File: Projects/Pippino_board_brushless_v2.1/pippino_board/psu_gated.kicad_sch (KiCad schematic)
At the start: 11 parts, among them Q1 2N3904, Q2 AO4409

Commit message: changed 5v buck to smaller one
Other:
- sheet PSU_5v0 ports: added 5V_EN; removed none
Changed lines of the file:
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@@
+    (stroke (width 0) (type default))
+  )
+  (wire (pts (xy 195.58 87.63) (xy 204.47 87.63))
     (stroke (width 0) (type default))
   )
@@
   (hierarchical_label "power_maintain" (shape input) (at 147.32 99.06 0) (fields_autoplaced)
     (effects (font (size 1.27 1.27)) (justify left))
+  )
+  (hierarchical_label "5V_EN" (shape input) (at 195.58 87.63 180) (fields_autoplaced)
+    (effects (font (size 1.27 1.27)) (justify right))
   )
   (hierarchical_label "trigger_manual" (shape input) (at 100.33 83.82 180) (fields_autoplaced)
@@
     )
   )
-  (sheet (at 204.47 81.28) (size 15.24 7.62) (fields_autoplaced)
+  (sheet (at 204.47 81.28) (size 15.24 10.16) (fields_autoplaced)
     (stroke (width 0.1524) (type solid))
     (fill (color 0 0 0 0.0000))
@@
       (effects (font (size 1.27 1.27)) (justify left bottom))
     )
-    (property "Sheetfile" "psu_5v0.kicad_sch" (at 204.47 89.4846 0)
+    (property "Sheetfile" "psu_5v0.kicad_sch" (at 204.47 92.0246 0)
       (effects (font (size 1.27 1.27)) (justify left top))
     )
@@
       (effects (font (size 1.27 1.27)) (justify left))
     )
+    (pin "5V_EN" input (at 204.47 87.63 180)
+      (effects (font (size 1.27 1.27)) (justify left))
+    )

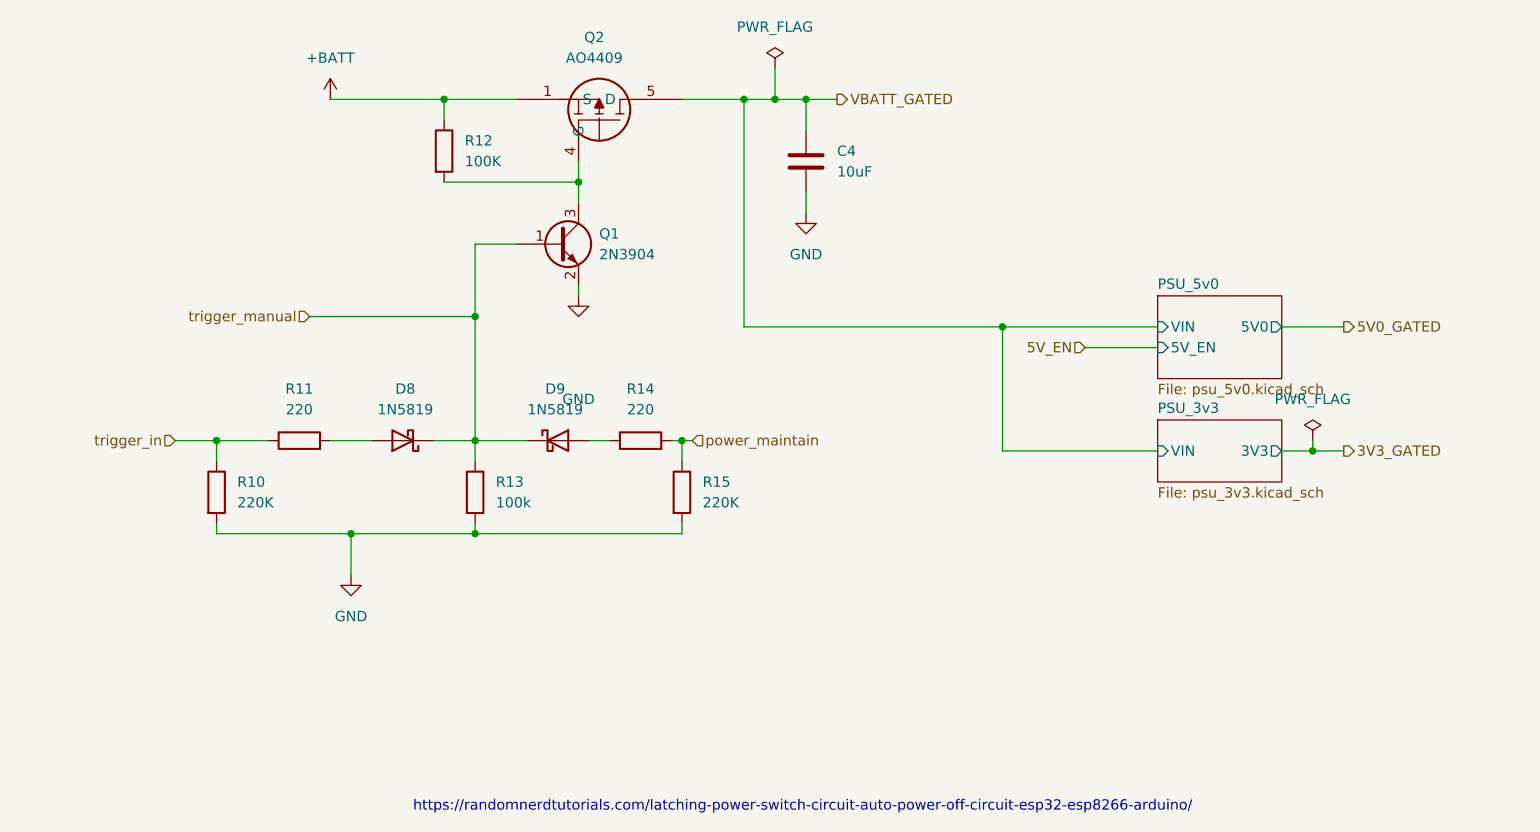
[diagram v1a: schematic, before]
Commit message: moved to ubu 22, updated pippino v2.1
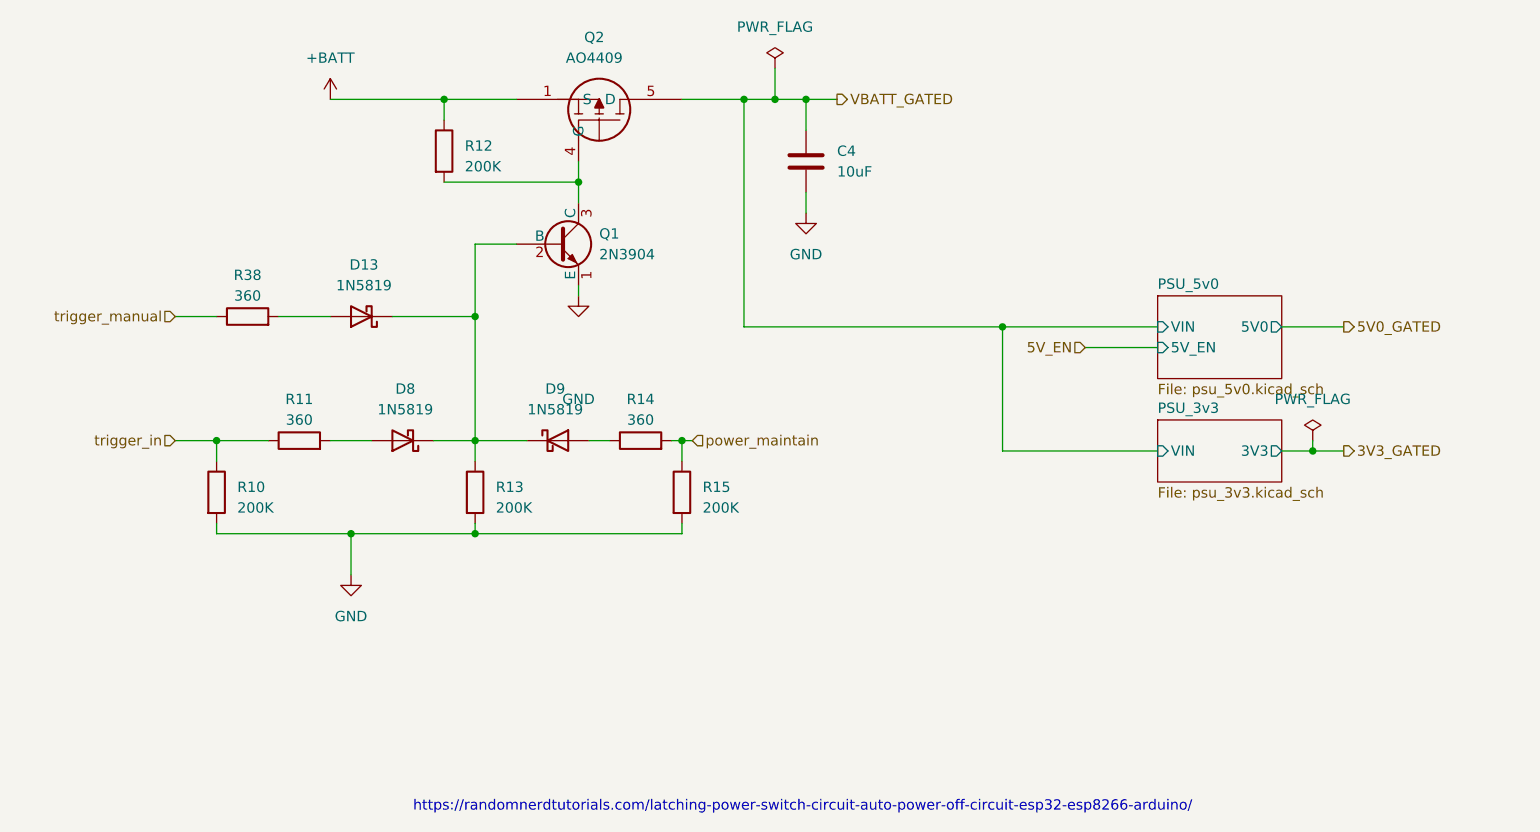
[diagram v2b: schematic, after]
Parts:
- added D13: 1N5819, Diode_SMD:D_SOD-123, symbol Diode:1N5819
- added R38: 360, Resistor_SMD:R_1206_3216Metric, symbol Device:R
- Q1: footprint Package_TO_SOT_SMD:SOT-23 -> Components:2N3904_SOT-23; symbol Custom_Components:2N3904_SMD -> Transistor_BJT:2N3904
- R10, R15: value 220K -> 200K
- R11, R14: value 220 -> 360
- R12: value 100K -> 200K
- R13: value 100k -> 200K
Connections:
- net GND: now also Q1.1 (E); no longer Q1.2 (E)
- net trigger_manual: now also R38.1; no longer D8.1 (K), D9.1 (K), Q1.1 (B), R13.1
- new net: D13.1 (K), D8.1 (K), D9.1 (K), Q1.2 (B), R13.1
- new net: D13.2 (A), R38.2
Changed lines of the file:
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@@
+    (stroke (width 0) (type default))
+  )
+  (wire (pts (xy 96.52 83.82) (xy 102.87 83.82))
     (stroke (width 0) (type default))
   )
@@
     (stroke (width 0) (type default))
   )
+  (wire (pts (xy 110.49 83.82) (xy 120.65 83.82))
+    (stroke (width 0) (type default))
+  )
   (wire (pts (xy 153.67 85.09) (xy 185.42 85.09))
     (stroke (width 0) (type default))
@@
     (stroke (width 0) (type default))
   )
-  (wire (pts (xy 100.33 83.82) (xy 120.65 83.82))
+  (wire (pts (xy 83.82 83.82) (xy 88.9 83.82))
     (stroke (width 0) (type default))
   )
@@
     (effects (font (size 1.27 1.27)) (justify right))
   )
-  (hierarchical_label "trigger_manual" (shape input) (at 100.33 83.82 180) (fields_autoplaced)
+  (hierarchical_label "trigger_manual" (shape input) (at 83.82 83.82 180) (fields_autoplaced)
     (effects (font (size 1.27 1.27)) (justify right))
   )
@@
   (symbol (lib_id "Device:R") (at 99.06 99.06 90) (unit 1)
     (in_bom yes) (on_board yes) (dnp no) (fields_autoplaced)
-    (property "Reference" "R11" (at 99.06 92.71 90)
-      (effects (font (size 1.27 1.27)))
-    )
-    (property "Value" "220" (at 99.06 95.25 90)
+    (property "Reference" "R11" (at 99.06 93.98 90)
+      (effects (font (size 1.27 1.27)))
+    )
+    (property "Value" "360" (at 99.06 96.52 90)
       (effects (font (size 1.27 1.27)))
     )
@@
   (symbol (lib_id "Device:R") (at 116.84 63.5 0) (unit 1)
     (in_bom yes) (on_board yes) (dnp no) (fields_autoplaced)
-    (property "Reference" "R12" (at 119.38 62.2299 0)
-      (effects (font (size 1.27 1.27)) (justify left))
-    )
-    (property "Value" "100K" (at 119.38 64.7699 0)
+    (property "Reference" "R12" (at 119.38 62.865 0)
+      (effects (font (size 1.27 1.27)) (justify left))
+    )
+    (property "Value" "200K" (at 119.38 65.405 0)
       (effects (font (size 1.27 1.27)) (justify left))
     )
@@
   (symbol (lib_id "Device:R") (at 140.97 99.06 90) (unit 1)
     (in_bom yes) (on_board yes) (dnp no) (fields_autoplaced)
-    (property "Reference" "R14" (at 140.97 92.71 90)
-      (effects (font (size 1.27 1.27)))
-    )
-    (property "Value" "220" (at 140.97 95.25 90)
+    (property "Reference" "R14" (at 140.97 93.98 90)
+      (effects (font (size 1.27 1.27)))
+    )
+    (property "Value" "360" (at 140.97 96.52 90)
       (effects (font (size 1.27 1.27)))
     )
@@
   (symbol (lib_id "Device:R") (at 120.65 105.41 0) (unit 1)
     (in_bom yes) (on_board yes) (dnp no) (fields_autoplaced)
-    (property "Reference" "R13" (at 123.19 104.1399 0)
-      (effects (font (size 1.27 1.27)) (justify left))
-    )
-    (property "Value" "100k" (at 123.19 106.6799 0)
+    (property "Reference" "R13" (at 123.19 104.775 0)
+      (effects (font (size 1.27 1.27)) (justify left))
+    )
+    (property "Value" "200K" (at 123.19 107.315 0)
       (effects (font (size 1.27 1.27)) (justify left))
     )
@@
     )
   )
-  (symbol (lib_id "Custom_Components:2N3904_SMD") (at 130.81 74.93 0) (unit 1)
+  (symbol (lib_id "Transistor_BJT:2N3904") (at 130.81 74.93 0) (unit 1)
     (in_bom yes) (on_board yes) (dnp no) (fields_autoplaced)
     (property "Reference" "Q1" (at 135.89 73.6599 0)
@@
       (effects (font (size 1.27 1.27)) (justify left))
     )
-    (property "Footprint" "Package_TO_SOT_SMD:SOT-23" (at 135.89 76.835 0)
+    (property "Footprint" "Components:2N3904_SOT-23" (at 135.89 76.835 0)
       (effects (font (size 1.27 1.27) italic) (justify left) hide)
     )
@@
     )
   )
+  (symbol (lib_id "Diode:1N5819") (at 106.68 83.82 180) (unit 1)
+    (in_bom yes) (on_board yes) (dnp no) (fields_autoplaced)
+    (property "Reference" "D13" (at 106.9975 77.47 0)
+      (effects (font (size 1.27 1.27)))
+    )
+    (property "Value" "1N5819" (at 106.9975 80.01 0)
+      (effects (font (size 1.27 1.27)))
+    )
+    (property "Footprint" "Diode_SMD:D_SOD-123" (at 106.68 79.375 0)
+      (effects (font (size 1.27 1.27)) hide)
+    )
+    (property "Datasheet" "http://www.vishay.com/docs/88525/1n5817.pdf" (at 106.68 83.82 0)
+      (effects (font (size 1.27 1.27)) hide)
+    )
+    (pin "1")
+    (pin "2")
+    (instances
+      (project "pippino_board"
+        (path "/dedb2da3-2254-430c-8837-0c4d082ac264/4b10fb5e-e57c-48de-8995-e07357b61829"
+          (reference "D13") (unit 1)
+        )
+      )
+    )
+  )
   (symbol (lib_id "Device:C") (at 161.29 64.77 0) (unit 1)
     (in_bom yes) (on_board yes) (dnp no) (fields_autoplaced)
@@
   (symbol (lib_id "Device:R") (at 88.9 105.41 0) (unit 1)
     (in_bom yes) (on_board yes) (dnp no) (fields_autoplaced)
-    (property "Reference" "R10" (at 91.44 104.1399 0)
-      (effects (font (size 1.27 1.27)) (justify left))
-    )
-    (property "Value" "220K" (at 91.44 106.6799 0)
+    (property "Reference" "R10" (at 91.44 104.775 0)
+      (effects (font (size 1.27 1.27)) (justify left))
+    )
+    (property "Value" "200K" (at 91.44 107.315 0)
       (effects (font (size 1.27 1.27)) (justify left))
     )
@@
   (symbol (lib_id "Device:R") (at 146.05 105.41 0) (unit 1)
     (in_bom yes) (on_board yes) (dnp no) (fields_autoplaced)
-    (property "Reference" "R15" (at 148.59 104.1399 0)
-      (effects (font (size 1.27 1.27)) (justify left))
-    )
-    (property "Value" "220K" (at 148.59 106.6799 0)
+    (property "Reference" "R15" (at 148.59 104.775 0)
+      (effects (font (size 1.27 1.27)) (justify left))
+    )
+    (property "Value" "200K" (at 148.59 107.315 0)
       (effects (font (size 1.27 1.27)) (justify left))
     )
@@
         )
       )
+    )
+  )
+  (symbol (lib_id "Device:R") (at 92.71 83.82 90) (unit 1)
+    (in_bom yes) (on_board yes) (dnp no) (fields_autoplaced)
+    (property "Reference" "R38" (at 92.71 78.74 90)
+      (effects (font (size 1.27 1.27)))
+    )
+    (property "Value" "360" (at 92.71 81.28 90)
+      (effects (font (size 1.27 1.27)))
+    )
+    (property "Footprint" "Resistor_SMD:R_1206_3216Metric" (at 92.71 85.598 90)
+      (effects (font (size 1.27 1.27)) hide)
+    )
+    (property "Datasheet" "~" (at 92.71 83.82 0)
+      (effects (font (size 1.27 1.27)) hide)
+    )
+    (pin "1")
+    (pin "2")
+    (instances
+      (project "pippino_board"
+        (path "/dedb2da3-2254-430c-8837-0c4d082ac264/4b10fb5e-e57c-48de-8995-e07357b61829"
+          (reference "R38") (unit 1)
+        )
+      )
